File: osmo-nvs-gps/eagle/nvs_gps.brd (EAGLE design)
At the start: 49.5 x 50 mm, 20 parts, among them K1 JACK2.5_SJ-2523, K2 JACK2.5_SJ-2523, U1 NV08C-CSM, X1 MOLEX_MCX_V

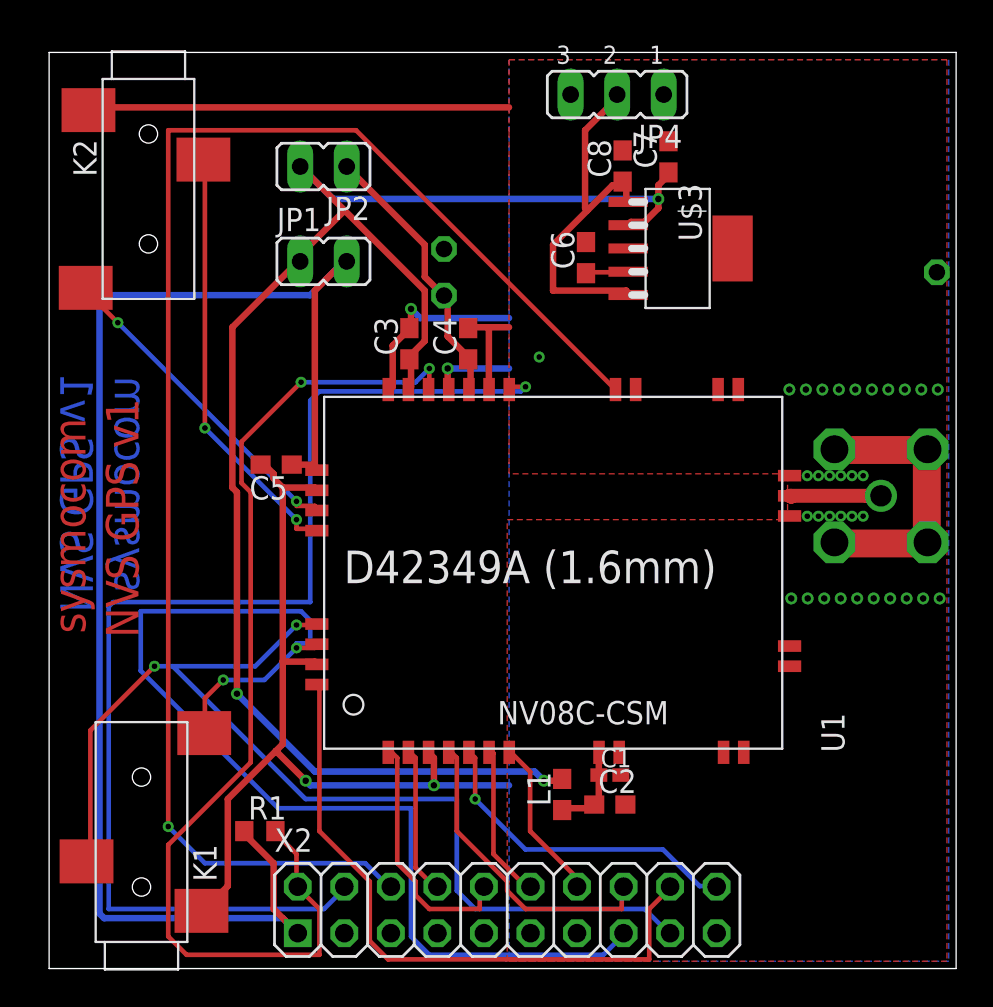
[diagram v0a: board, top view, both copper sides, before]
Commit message: add a power-indicator LED to the NVS board and tag it v2
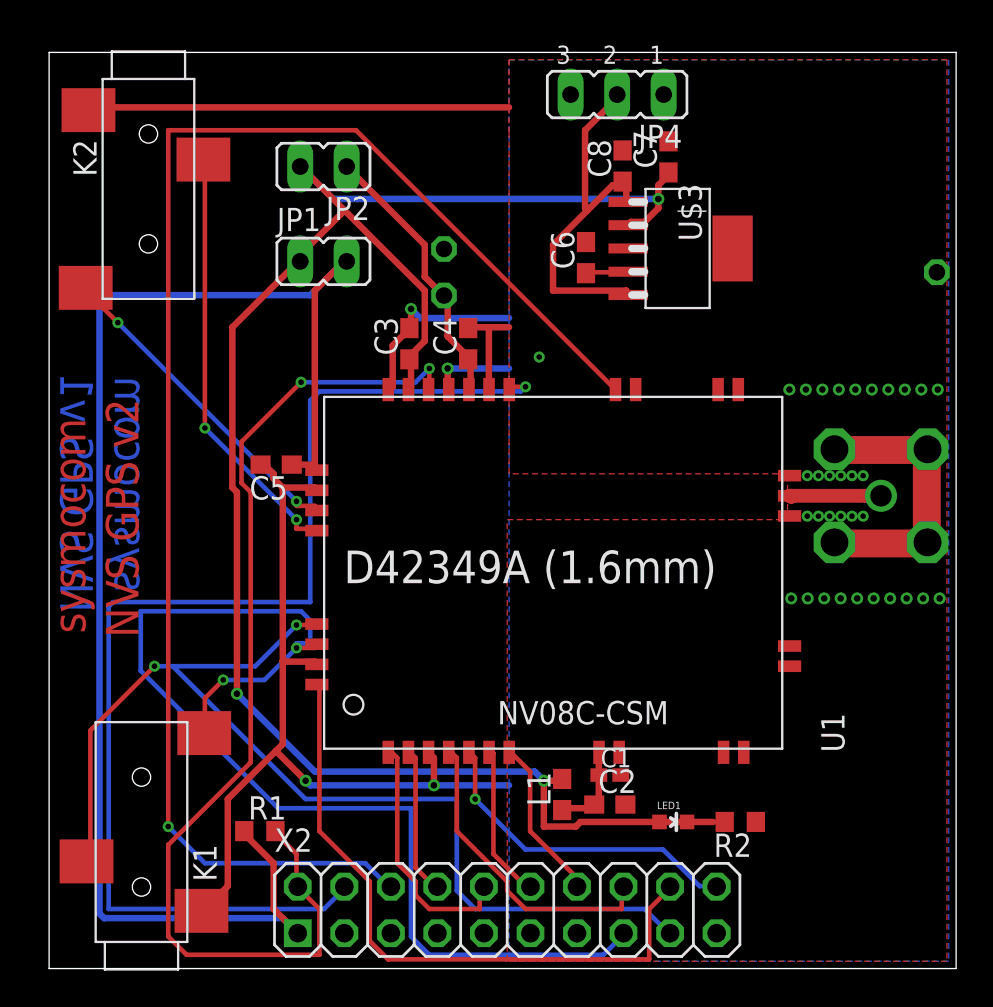
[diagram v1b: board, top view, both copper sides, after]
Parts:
- added LED1: (no value), SparkFun-LED:LED-0603
- added R2: (no value), rcl:R0603
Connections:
- new net N$14: LED1.C, R2.2
- net GND: now also R2.1
- net VIN_D: now also LED1.A
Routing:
- net VIN_D: track 88.7 -> 100.5 mm
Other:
- board text added: "NVS GPS v2"
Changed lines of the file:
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@@
 <layer number="48" name="Document" color="7" fill="1" visible="yes" active="yes"/>
 <layer number="49" name="Reference" color="7" fill="1" visible="yes" active="yes"/>
+<layer number="50" name="dxf" color="7" fill="1" visible="no" active="no"/>
 <layer number="51" name="tDocu" color="7" fill="1" visible="yes" active="yes"/>
 <layer number="52" name="bDocu" color="7" fill="1" visible="yes" active="yes"/>
+<layer number="53" name="tGND_GNDA" color="7" fill="9" visible="no" active="no"/>
+<layer number="54" name="bGND_GNDA" color="1" fill="9" visible="no" active="no"/>
+<layer number="56" name="wert" color="7" fill="1" visible="no" active="no"/>
 <layer number="91" name="Nets" color="2" fill="1" visible="no" active="no"/>
 <layer number="92" name="Busses" color="1" fill="1" visible="no" active="no"/>
@@
 <layer number="97" name="Info" color="7" fill="1" visible="no" active="no"/>
 <layer number="98" name="Guide" color="6" fill="1" visible="no" active="no"/>
+<layer number="100" name="Muster" color="7" fill="1" visible="no" active="no"/>
+<layer number="101" name="Patch_Top" color="12" fill="4" visible="no" active="yes"/>
+<layer number="102" name="Vscore" color="7" fill="1" visible="no" active="yes"/>
+<layer number="103" name="tMap" color="7" fill="1" visible="no" active="yes"/>
+<layer number="104" name="Name" color="16" fill="1" visible="no" active="yes"/>
+<layer number="105" name="tPlate" color="7" fill="1" visible="no" active="yes"/>
+<layer number="106" name="bPlate" color="7" fill="1" visible="no" active="yes"/>
+<layer number="107" name="Crop" color="7" fill="1" visible="no" active="yes"/>
+<layer number="116" name="Patch_BOT" color="9" fill="4" visible="no" active="yes"/>
+<layer number="121" name="_tsilk" color="7" fill="1" visible="no" active="yes"/>
+<layer number="122" name="_bsilk" color="7" fill="1" visible="no" active="yes"/>
+<layer number="125" name="_tNames" color="7" fill="1" visible="no" active="yes"/>
+<layer number="144" name="Drill_legend" color="7" fill="1" visible="no" active="yes"/>
+<layer number="151" name="HeatSink" color="7" fill="1" visible="no" active="yes"/>
+<layer number="200" name="200bmp" color="1" fill="10" visible="no" active="yes"/>
+<layer number="201" name="201bmp" color="2" fill="10" visible="no" active="yes"/>
+<layer number="202" name="202bmp" color="3" fill="10" visible="no" active="yes"/>
+<layer number="203" name="203bmp" color="4" fill="10" visible="no" active="yes"/>
+<layer number="204" name="204bmp" color="5" fill="10" visible="no" active="yes"/>
+<layer number="205" name="205bmp" color="6" fill="10" visible="no" active="yes"/>
+<layer number="206" name="206bmp" color="7" fill="10" visible="no" active="yes"/>
+<layer number="207" name="207bmp" color="8" fill="10" visible="no" active="yes"/>
+<layer number="208" name="208bmp" color="9" fill="10" visible="no" active="yes"/>
+<layer number="209" name="209bmp" color="7" fill="1" visible="no" active="yes"/>
+<layer number="210" name="210bmp" color="7" fill="1" visible="no" active="yes"/>
+<layer number="211" name="211bmp" color="7" fill="1" visible="no" active="yes"/>
+<layer number="212" name="212bmp" color="7" fill="1" visible="no" active="yes"/>
+<layer number="213" name="213bmp" color="7" fill="1" visible="no" active="yes"/>
+<layer number="214" name="214bmp" color="7" fill="1" visible="no" active="yes"/>
+<layer number="215" name="215bmp" color="7" fill="1" visible="no" active="yes"/>
+<layer number="216" name="216bmp" color="7" fill="1" visible="no" active="yes"/>
+<layer number="217" name="217bmp" color="18" fill="1" visible="no" active="no"/>
+<layer number="218" name="218bmp" color="19" fill="1" visible="no" active="no"/>
+<layer number="219" name="219bmp" color="20" fill="1" visible="no" active="no"/>
+<layer number="220" name="220bmp" color="21" fill="1" visible="no" active="no"/>
+<layer number="221" name="221bmp" color="22" fill="1" visible="no" active="no"/>
+<layer number="222" name="222bmp" color="23" fill="1" visible="no" active="no"/>
+<layer number="223" name="223bmp" color="24" fill="1" visible="no" active="no"/>
+<layer number="224" name="224bmp" color="25" fill="1" visible="no" active="no"/>
+<layer number="250" name="Descript" color="3" fill="1" visible="no" active="no"/>
+<layer number="251" name="SMDround" color="12" fill="11" visible="no" active="no"/>
+<layer number="254" name="cooling" color="7" fill="1" visible="no" active="yes"/>
 </layers>
 <board>
@@
 <text x="3.5814" y="20.574" size="1.778" layer="16" rot="MR90">sysmocom</text>
 <text x="0.6096" y="19.431" size="1.778" layer="16" rot="MR90">NVS GPS v1</text>
-<text x="4.8768" y="18.0594" size="1.778" layer="1" rot="R90">NVS GPS v1</text>
+<text x="4.8768" y="18.0594" size="1.778" layer="1" rot="R90">NVS GPS v2</text>
 <text x="16.0782" y="21.0312" size="1.778" layer="21">D42349A (1.6mm)</text>
 </plain>
@@
 <element name="C8" library="rcl" package="C0603" value="10u" x="31.300025" y="43.800034375" rot="R90"/>
 <element name="JP4" library="jumper" package="JP2" value="" x="31.0000125" y="47.700009375" rot="R180"/>
+<element name="LED1" library="SparkFun-LED" package="LED-0603" value="" x="34.0614" y="8.001" rot="R270"/>
+<element name="R2" library="rcl" package="R0603" value="" x="37.719" y="8.001" rot="R180"/>
 </elements>
 <signals>
@@
 <via x="14" y="10.25" extent="1-16" drill="0.3556"/>
 <via x="26.7462" y="33.3756" extent="1-16" drill="0.3048" shape="octagon"/>
+<contactref element="R2" pad="1"/>
 </signal>
 <signal name="RF" class="2">
@@
 <via x="27" y="10.25" extent="1-16" drill="0.3556"/>
 <via x="10.25" y="15" extent="1-16" drill="0.3556"/>
+<contactref element="LED1" pad="A"/>
+<wire x1="28.75" y1="7.75" x2="29" y2="8" width="0.3556" layer="1"/>
+<wire x1="27" y1="7.75" x2="28.75" y2="7.75" width="0.3556" layer="1"/>
+<wire x1="27" y1="10.25" x2="27" y2="7.75" width="0.3556" layer="1"/>
+<wire x1="36.25" y1="8" x2="33.3114" y2="8.001" width="0.3556" layer="1"/>
+<wire x1="29" y1="8" x2="33.25" y2="8" width="0.3556" layer="1"/>
+<wire x1="33.25" y1="8" x2="33.3114" y2="8.001" width="0.3556" layer="1"/>
 </signal>
 <signal name="N$7" class="1">
@@
 <wire x1="29.25" y1="41.5" x2="29.375" y2="41.375" width="0.3556" layer="1"/>
 </signal>
+<signal name="N$14">
+<contactref element="R2" pad="2"/>
+<contactref element="LED1" pad="C"/>
+<wire x1="34.8114" y1="8.001" x2="36.869" y2="8.001" width="0" layer="19" extent="1-1"/>
+</signal>
 </signals>
-<errors>
-</errors>
 </board>
 </drawing>

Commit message: avoid short-circuit of power LED
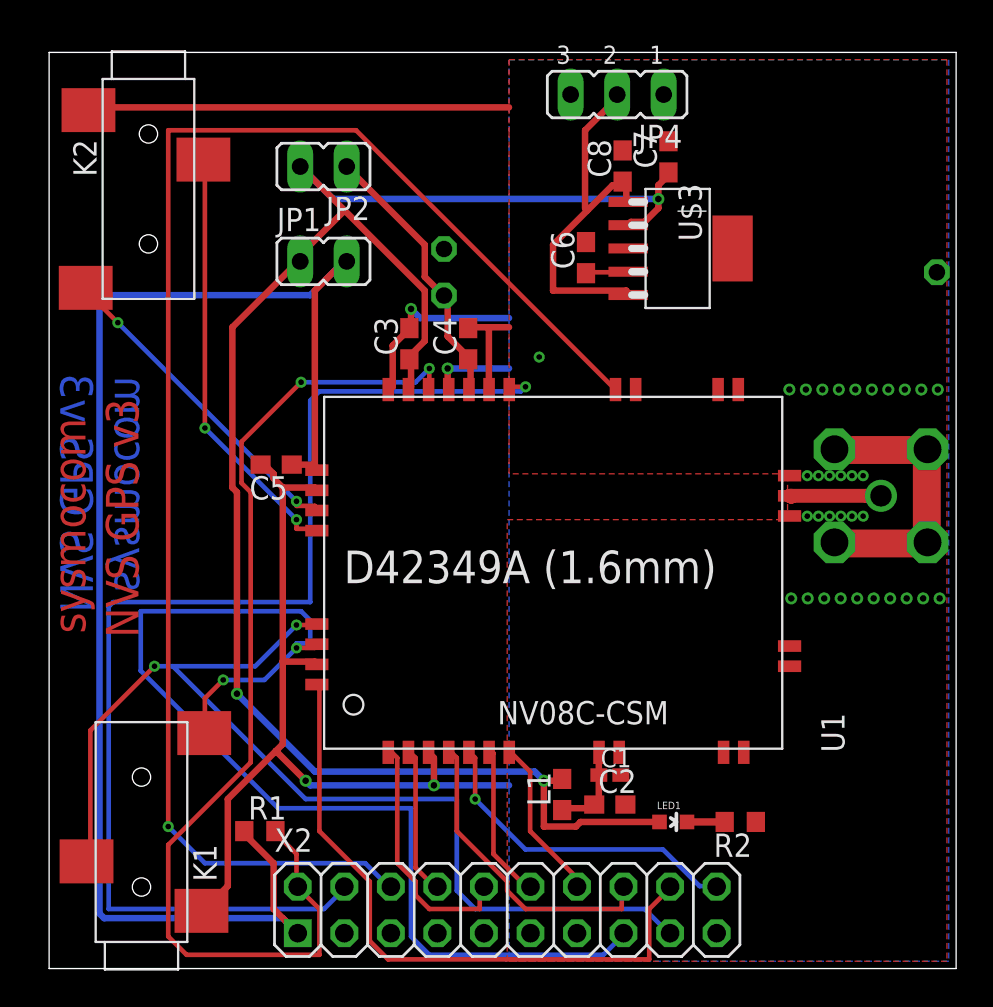
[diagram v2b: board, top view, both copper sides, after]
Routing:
- net VIN_D: track 100.5 -> 97.6 mm
- net N$14: track 0.00 -> 2.06 mm
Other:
- board text added: "NVS GPS v3"
- board text removed: "NVS GPS v1"
- board text removed: "NVS GPS v2"
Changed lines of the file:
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@@
 <?xml version="1.0" encoding="utf-8"?>
 <!DOCTYPE eagle SYSTEM "eagle.dtd">
-<eagle version="6.0">
+<eagle version="6.4">
 <drawing>
 <settings>
@@
 <text x="1.9812" y="18.288" size="1.778" layer="1" rot="R90">sysmocom</text>
 <text x="3.5814" y="20.574" size="1.778" layer="16" rot="MR90">sysmocom</text>
-<text x="0.6096" y="19.431" size="1.778" layer="16" rot="MR90">NVS GPS v1</text>
-<text x="4.8768" y="18.0594" size="1.778" layer="1" rot="R90">NVS GPS v2</text>
+<text x="0.6096" y="19.431" size="1.778" layer="16" rot="MR90">NVS GPS v3</text>
+<text x="4.8768" y="18.0594" size="1.778" layer="1" rot="R90">NVS GPS v3</text>
 <text x="16.0782" y="21.0312" size="1.778" layer="21">D42349A (1.6mm)</text>
 </plain>
@@
 </class>
 </classes>
-<designrules>
+<designrules name="default">
 <description language="de">&lt;b&gt;EAGLE Design Rules&lt;/b&gt;
 &lt;p&gt;
@@
 <wire x1="27" y1="7.75" x2="28.75" y2="7.75" width="0.3556" layer="1"/>
 <wire x1="27" y1="10.25" x2="27" y2="7.75" width="0.3556" layer="1"/>
-<wire x1="36.25" y1="8" x2="33.3114" y2="8.001" width="0.3556" layer="1"/>
 <wire x1="29" y1="8" x2="33.25" y2="8" width="0.3556" layer="1"/>
 <wire x1="33.25" y1="8" x2="33.3114" y2="8.001" width="0.3556" layer="1"/>
@@
 <contactref element="R2" pad="2"/>
 <contactref element="LED1" pad="C"/>
-<wire x1="34.8114" y1="8.001" x2="36.869" y2="8.001" width="0" layer="19" extent="1-1"/>
+<wire x1="36.869" y1="8.001" x2="34.8114" y2="8.001" width="0.4064" layer="1"/>
 </signal>
 </signals>
